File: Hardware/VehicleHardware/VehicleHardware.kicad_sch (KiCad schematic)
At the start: 12 parts, among them U1 LM7805_TO220, U2 ESP32-CAM, U3 L298HN

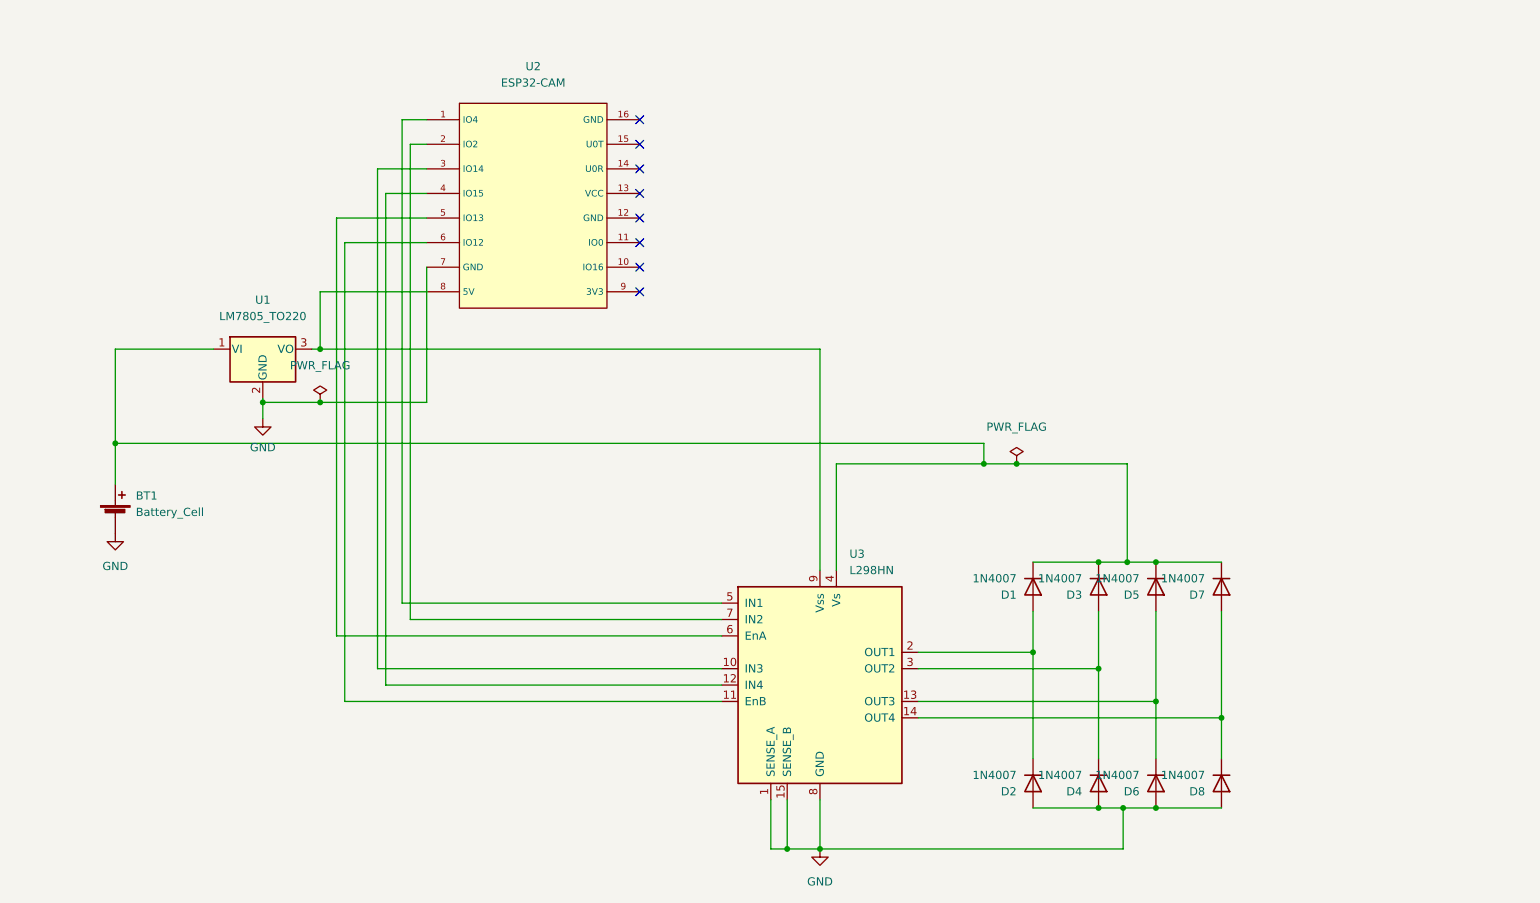
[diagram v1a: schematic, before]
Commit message: updated pcb and schematic;added header connectors;did some routing
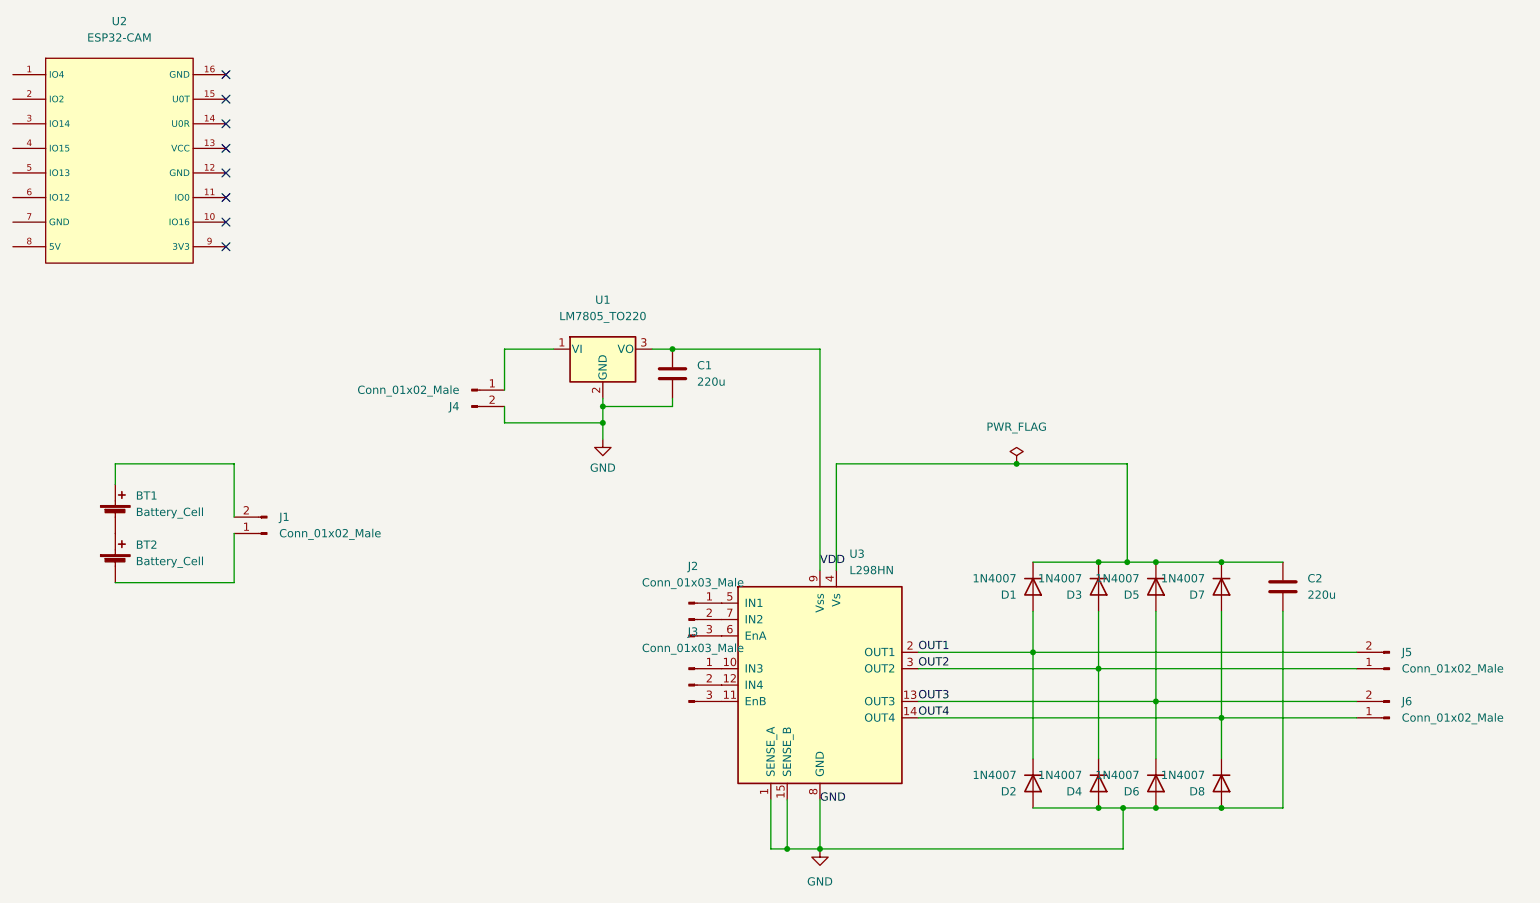
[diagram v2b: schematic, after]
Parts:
- added BT2: Battery_Cell, Battery:BatteryHolder_MPD_BH-18650-PC2, symbol Device:Battery_Cell
- added C1, C2: 220u, Capacitor_SMD:CP_Elec_3x5.3, symbol Device:C
- added J1, J4, J5, J6: Conn_01x02_Male, Connector_PinHeader_1.00mm:PinHeader_1x02_P1.00mm_Vertical, symbol Connector:Conn_01x02_Male
- added J2, J3: Conn_01x03_Male, Connector_PinHeader_1.00mm:PinHeader_1x03_P1.00mm_Vertical, symbol Connector:Conn_01x03_Male
- BT1: footprint Battery:BatteryHolder_Keystone_1042_1x18650 -> Battery:BatteryHolder_MPD_BH-18650-PC2
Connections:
- net GND: now also C1.2, C2.2, J4.2 (Pin_2); no longer BT1.2 (-), U2.7 (GND)
- net at D1.1 (K), D3.1 (K), D5.1 (K)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: now also C2.1; no longer BT1.1 (+), U1.1 (VI)
- net OUT2: now reaches D3.2 (A), D4.1 (K), U3.3 (OUT2)
- net OUT2: now also J5.1 (Pin_1)
- net OUT4: now reaches D7.2 (A), D8.1 (K), U3.14 (OUT4)
- net OUT4: now also J6.1 (Pin_1)
- net OUT1: now reaches D1.2 (A), D2.1 (K), U3.2 (OUT1)
- net OUT1: now also J5.2 (Pin_2)
- net at U3.10 (IN3): now also J3.1 (Pin_1); no longer U2.3 (IO14)
- net at U3.11 (EnB): now also J3.3 (Pin_3); no longer U2.6 (IO12)
- net at U3.12 (IN4): now also J3.2 (Pin_2); no longer U2.4 (IO15)
- net OUT3: now reaches D5.2 (A), D6.1 (K), U3.13 (OUT3)
- net OUT3: now also J6.2 (Pin_2)
- net at U3.5 (IN1): now also J2.1 (Pin_1); no longer U2.1 (IO4)
- net at U3.6 (EnA): now also J2.3 (Pin_3); no longer U2.5 (IO13)
- net at U3.7 (IN2): now also J2.2 (Pin_2); no longer U2.2 (IO2)
- net VDD: now reaches U1.3 (VO), U3.9 (Vss)
- net VDD: now also C1.1; no longer U2.8 (5V)
- new net: BT2.2 (-), J1.1 (Pin_1)
- new net: BT1.1 (+), J1.2 (Pin_2)
- new net: J4.1 (Pin_1), U1.1 (VI)
- new net: BT1.2 (-), BT2.1 (+)
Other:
- moved on the sheet: U1, U2
